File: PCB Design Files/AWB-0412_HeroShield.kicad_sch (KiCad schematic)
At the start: 19 parts, among them J1 Power, J2 Digital/PWM, J3 Analog, J4 Digital/PWM, SW1 SW_Push, SW2 SW_Push, SW3 SW_Push, SW4 SW_Push, SW5 SW_Push_DPDT, SW6 SW_DIP_x02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

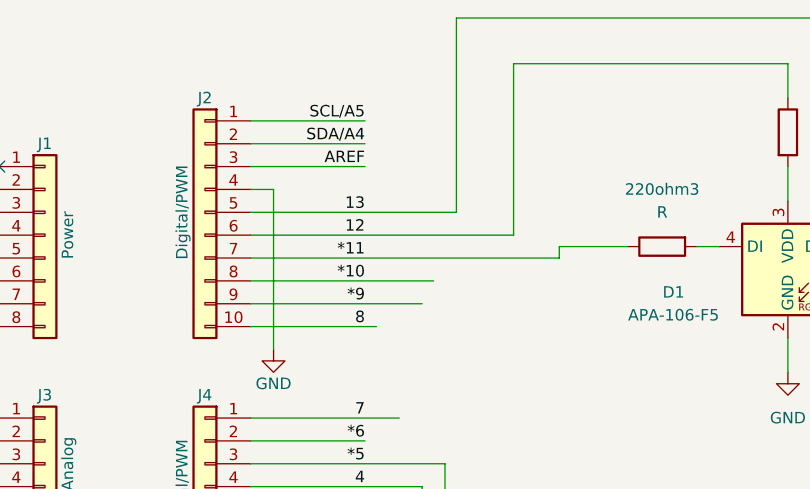
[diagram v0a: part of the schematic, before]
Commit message: Update PCB files
Updated the PCB files. Altered LED connections to ensure analog out compatible pins were connected to the LED. As well as added a JST PH 2-Pin connector for providing power.
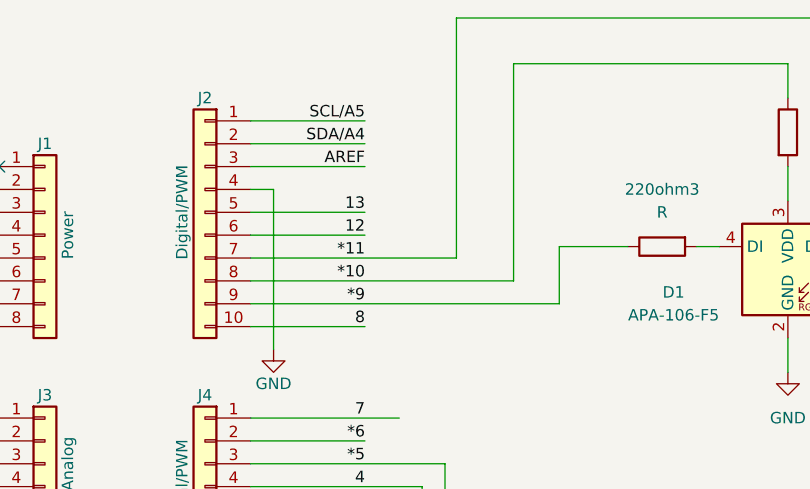
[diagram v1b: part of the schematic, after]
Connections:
- net *10: now also 220ohm2.1
- net *11: now also 220ohm1.1; no longer 220ohm3.1
- net *9: now also 220ohm3.1
- net 12: no longer 220ohm2.1
- net 13: no longer 220ohm1.1
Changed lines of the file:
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@@
     (stroke (width 0) (type solid) (color 0 0 0 0))
   )
-  (wire (pts (xy 62.23 44.45) (xy 82.55 44.45))
-    (stroke (width 0) (type solid) (color 0 0 0 0))
+  (wire (pts (xy 62.23 49.53) (xy 74.93 49.53))
+    (stroke (width 0) (type default) (color 0 0 0 0))
+  )
+  (wire (pts (xy 62.23 44.45) (xy 91.44 44.45))
+    (stroke (width 0) (type default) (color 0 0 0 0))
   )
   (wire (pts (xy 127 68.58) (xy 109.22 68.58))
@@
     (stroke (width 0) (type default) (color 0 0 0 0))
   )
-  (wire (pts (xy 96.52 40.64) (xy 96.52 41.91))
+  (wire (pts (xy 96.52 40.64) (xy 96.52 46.99))
     (stroke (width 0) (type default) (color 0 0 0 0))
   )
@@
     (stroke (width 0) (type solid) (color 0 0 0 0))
   )
-  (wire (pts (xy 62.23 39.37) (xy 91.44 39.37))
-    (stroke (width 0) (type solid) (color 0 0 0 0))
+  (wire (pts (xy 62.23 41.91) (xy 85.09 41.91))
+    (stroke (width 0) (type default) (color 0 0 0 0))
   )
   (wire (pts (xy 55.88 157.48) (xy 77.47 157.48))
@@
     (stroke (width 0) (type default) (color 0 0 0 0))
   )
-  (wire (pts (xy 62.23 36.83) (xy 85.09 36.83))
-    (stroke (width 0) (type default) (color 0 0 0 0))
-  )
   (wire (pts (xy 55.88 114.3) (xy 55.88 110.49))
     (stroke (width 0) (type default) (color 0 0 0 0))
@@
     (stroke (width 0) (type default) (color 0 0 0 0))
   )
-  (wire (pts (xy 62.23 46.99) (xy 81.28 46.99))
-    (stroke (width 0) (type solid) (color 0 0 0 0))
+  (wire (pts (xy 62.23 46.99) (xy 96.52 46.99))
+    (stroke (width 0) (type default) (color 0 0 0 0))
   )
   (wire (pts (xy 109.22 83.82) (xy 109.22 74.93))
@@
     (stroke (width 0) (type default) (color 0 0 0 0))
   )
-  (wire (pts (xy 85.09 15.24) (xy 85.09 36.83))
+  (wire (pts (xy 85.09 15.24) (xy 85.09 41.91))
     (stroke (width 0) (type default) (color 0 0 0 0))
   )
@@
     (stroke (width 0) (type default) (color 0 0 0 0))
   )
-  (wire (pts (xy 62.23 41.91) (xy 96.52 41.91))
-    (stroke (width 0) (type default) (color 0 0 0 0))
-  )
   (wire (pts (xy 64.77 34.29) (xy 64.77 52.07))
     (stroke (width 0) (type solid) (color 0 0 0 0))
@@
     (stroke (width 0) (type default) (color 0 0 0 0))
   )
-  (wire (pts (xy 91.44 20.32) (xy 91.44 39.37))
+  (wire (pts (xy 91.44 20.32) (xy 91.44 44.45))
     (stroke (width 0) (type default) (color 0 0 0 0))
   )
@@
     (stroke (width 0) (type solid) (color 0 0 0 0))
   )
+  (wire (pts (xy 62.23 39.37) (xy 74.93 39.37))
+    (stroke (width 0) (type default) (color 0 0 0 0))
+  )
   (wire (pts (xy 45.72 127) (xy 45.72 114.3))
     (stroke (width 0) (type default) (color 0 0 0 0))
@@
     (stroke (width 0) (type solid) (color 0 0 0 0))
   )
+  (wire (pts (xy 62.23 36.83) (xy 74.93 36.83))
+    (stroke (width 0) (type default) (color 0 0 0 0))
+  )
   (wire (pts (xy 62.23 69.85) (xy 77.47 69.85))
     (stroke (width 0) (type solid) (color 0 0 0 0))
@@
     (stroke (width 0) (type default) (color 0 0 0 0))
   )
-  (wire (pts (xy 62.23 49.53) (xy 76.2 49.53))
-    (stroke (width 0) (type solid) (color 0 0 0 0))
-  )
   (text "* Indicates a PWM-capable pin" (at 177.8 180.34 0)
